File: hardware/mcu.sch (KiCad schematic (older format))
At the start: 39 parts, among them J1 Micro_SD_Card, J2 BOOT0, J3 Conn_01x04_Male, J5 Conn_01x03_Male, J6 display, SW1 SW_right, SW2 SW_right, SW3 SW_top, SW4 SW_middle, SW5 SW_bot, SW6 SW_Left, SW7 SW_middle2, U1 STM32F042C6Tx

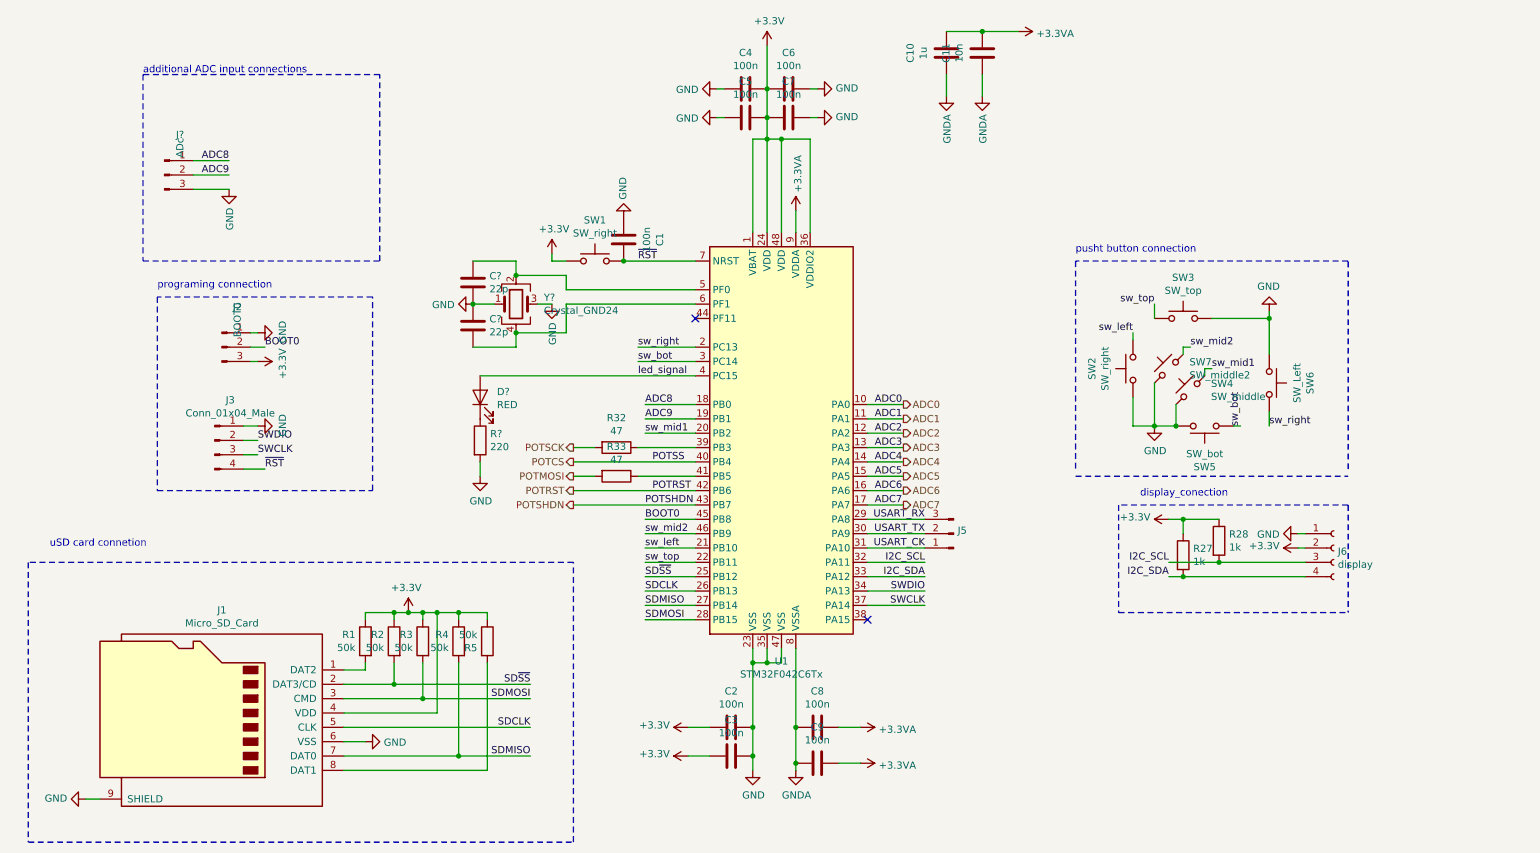
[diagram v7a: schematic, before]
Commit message: dodanie zabezpieczen portów i dzialniki napiec na wejsciach adc
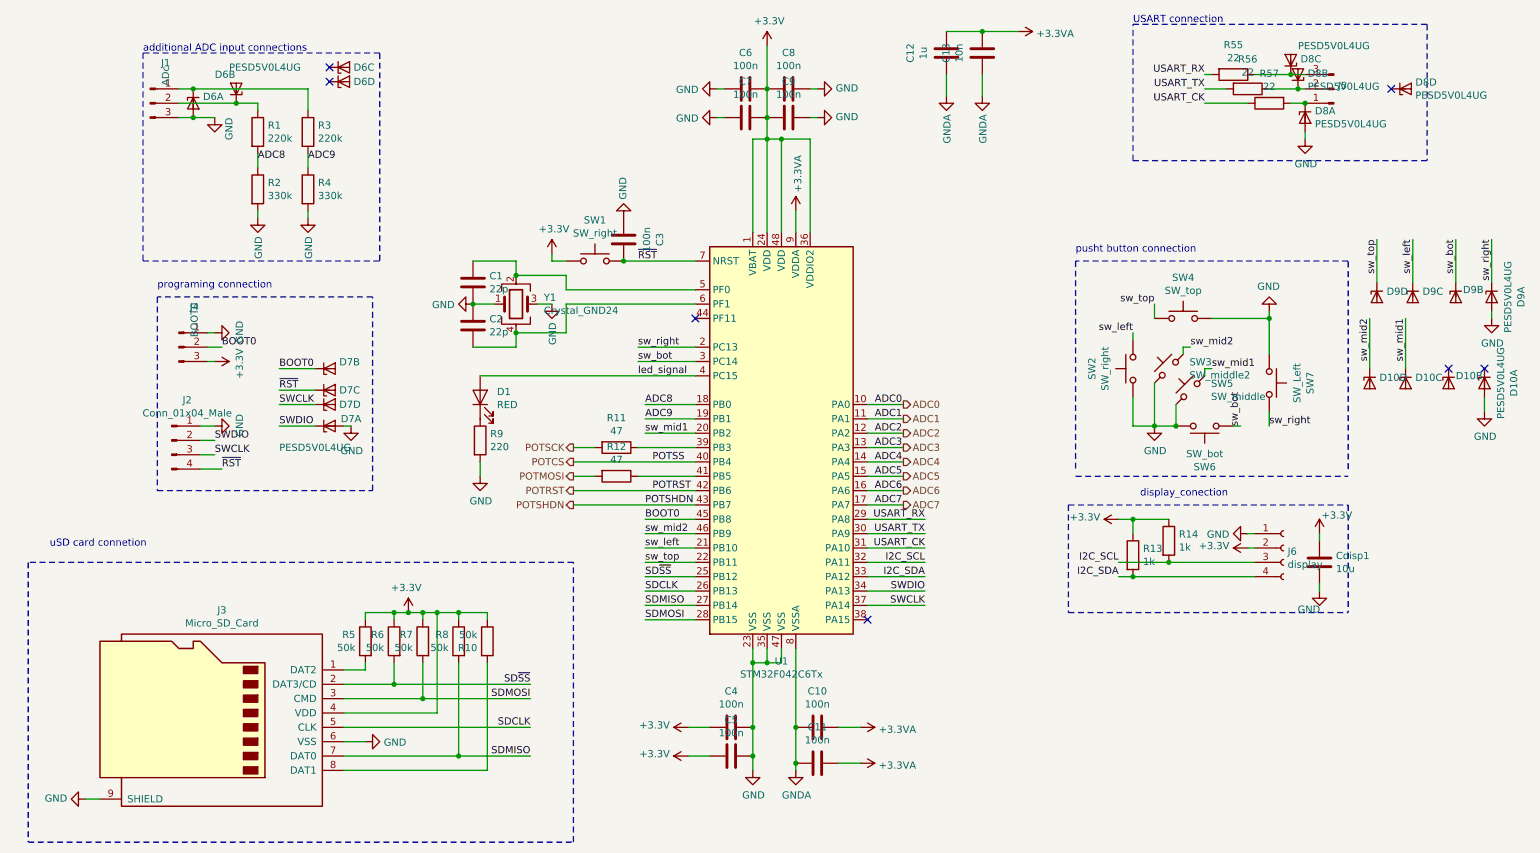
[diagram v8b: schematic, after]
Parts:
- added Cdisp1: 10u, Capacitor_SMD:C_0805_2012Metric, symbol Device:C
- added D10, D6, D7, D8, D9: PESD5V0L4UG, Package_TO_SOT_SMD:SOT-353_SC-70-5, symbol Power_Protection:PESD5V0L4UG
- added R1, R3: 220k, Resistor_SMD:R_0603_1608Metric_Pad1.05x0.95mm_HandSolder, symbol Device:R
- added R2, R4: 330k, Resistor_SMD:R_0603_1608Metric_Pad1.05x0.95mm_HandSolder, symbol Device:R
- added R55, R56, R57: 22, Resistor_SMD:R_0603_1608Metric_Pad1.05x0.95mm_HandSolder, symbol Device:R
- C1, C2: renamed from C?; footprint (none) -> Capacitor_SMD:C_0402_1005Metric
- J3: renamed from J1; footprint Connector_Card:microSD_HC_Hirose_DM3AT-SF-PEJM5 -> symbols:MOLEX_503398-1892
- Y1: renamed from Y?; footprint (none) -> Crystal:Crystal_SMD_3225-4Pin_3.2x2.5mm
- gave numbers to parts that had none: 3
- renumbered C8 to C10, C9 to C11, C10 to C12, C11 to C13, C1 to C3, C2 to C4, C3 to C5, C4 to C6, C5 to C7, C6 to C8, C7 to C9, J3 to J2, J2 to J4, R5 to R10, R32 to R11, R33 to R12, R27 to R13, R28 to R14, R1 to R5, R2 to R6, R3 to R7, R4 to R8, SW7 to SW3, SW3 to SW4, SW4 to SW5, SW5 to SW6, SW6 to SW7
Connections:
- net +3V3: now also Cdisp1.1
- net ADC8: now also R1.2, R2.1; no longer J1.1 (Pin_1)
- net ADC9: now also R3.2, R4.1; no longer J1.2 (Pin_2)
- net BOOT0: now also D7.3 (K2)
- net GND: now also Cdisp1.2, D10.2 (A), D6.2 (A), D7.2 (A), D8.2 (A), D9.2 (A), R2.2, R4.2
- net SWCLK: now also D7.6 (K4)
- net SWDIO: now also D7.1 (K1)
- net USART_CK: now also R57.1; no longer J5.1 (Pin_1)
- net USART_RX: now also R55.2; no longer J5.3 (Pin_3)
- net USART_TX: now also R56.2; no longer J5.2 (Pin_2)
- net sw_bot: now also D9.3 (K2)
- net sw_left: now also D9.4 (K3)
- net sw_mid1: now also D10.4 (K3)
- net sw_mid2: now also D10.6 (K4)
- net sw_right: now also D9.1 (K1)
- net sw_top: now also D9.6 (K4)
- net ~RST: now also D7.4 (K3)
- new net: D6.1 (K1), J1.1 (Pin_1), R3.1
- new net: D6.3 (K2), J1.2 (Pin_2), R1.1
- new net: D8.1 (K1), J5.1 (Pin_1), R57.2
- new net: D8.3 (K2), J5.2 (Pin_2), R56.1
- new net: D8.4 (K3), J5.3 (Pin_3), R55.1
- no-connect marks 2 -> 7
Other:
- note added: "USART connection\n"
- moved on the sheet: J1, J2, J4, J5, J6, R13, R14
